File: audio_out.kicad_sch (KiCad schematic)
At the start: 34 parts, among them SW2 Gain0, SW3 Gain1, U3 AP7333-33SR, U4 PCM5102A, U5 PAM8908JER

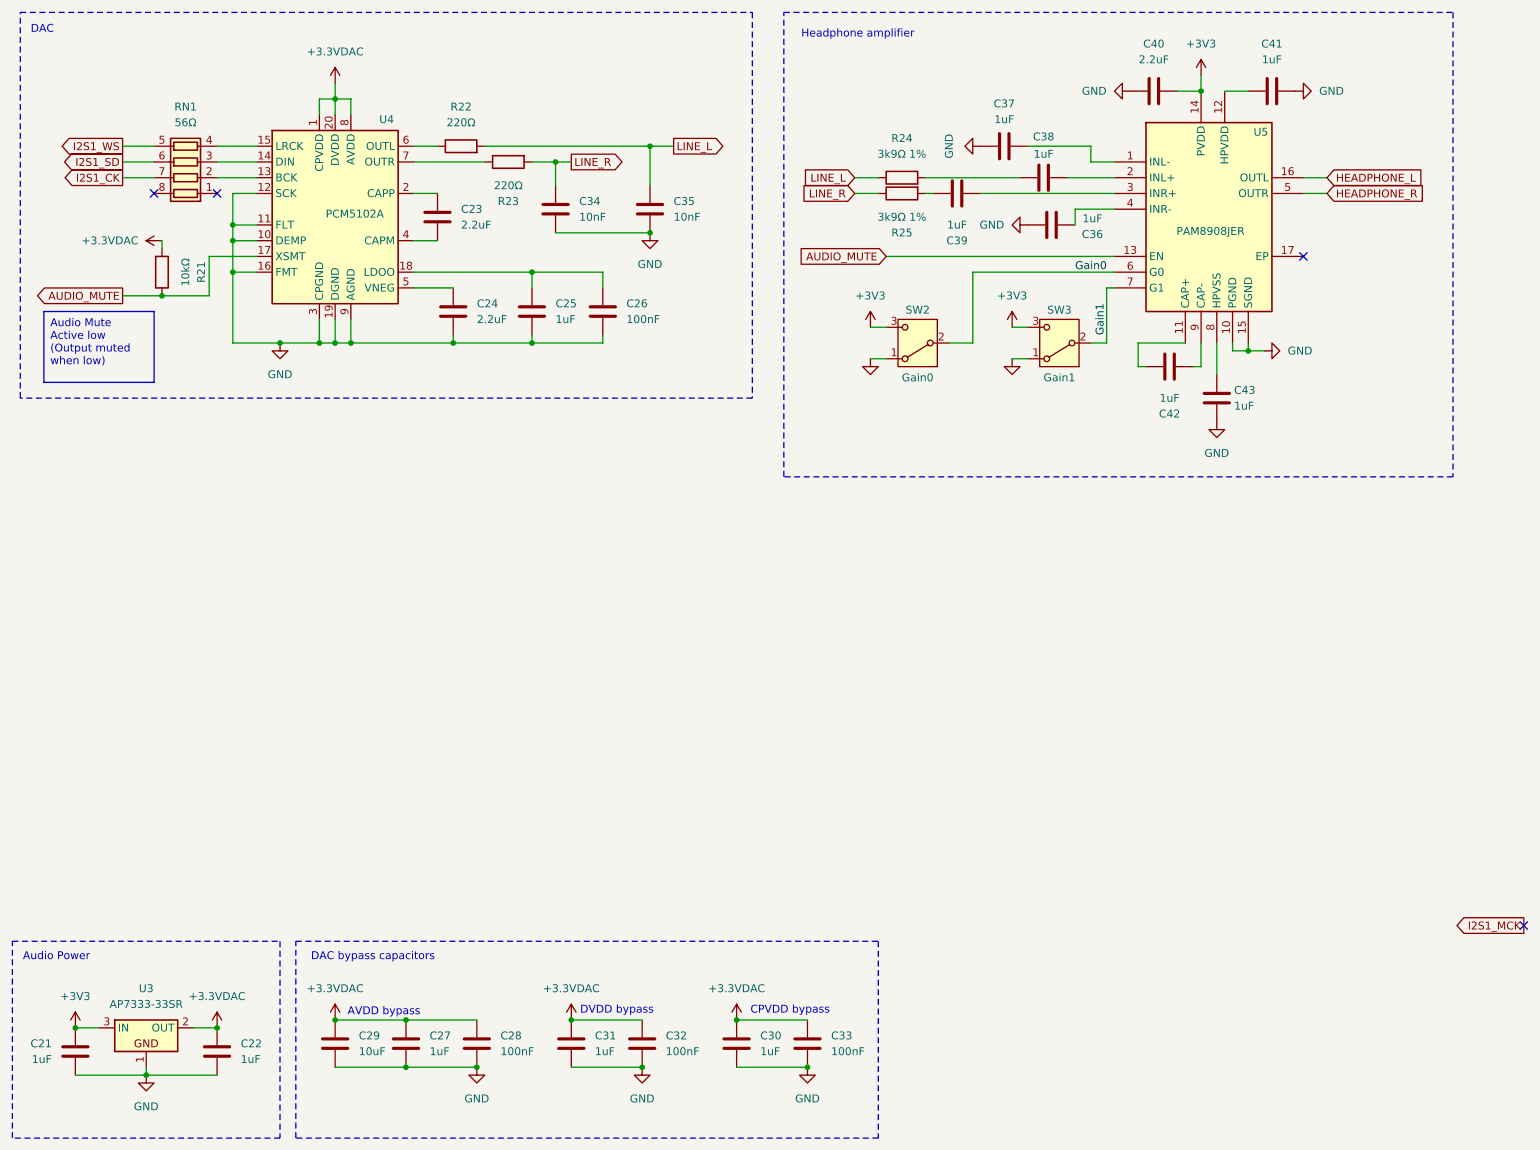
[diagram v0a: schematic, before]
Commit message: Updated schematic with parts found in JLCPCB parts database. Updated footprints, 3d models for those items. All schematic symbols now have LCSC part numbers, footprints and 3D models. No PCB layout has been done.
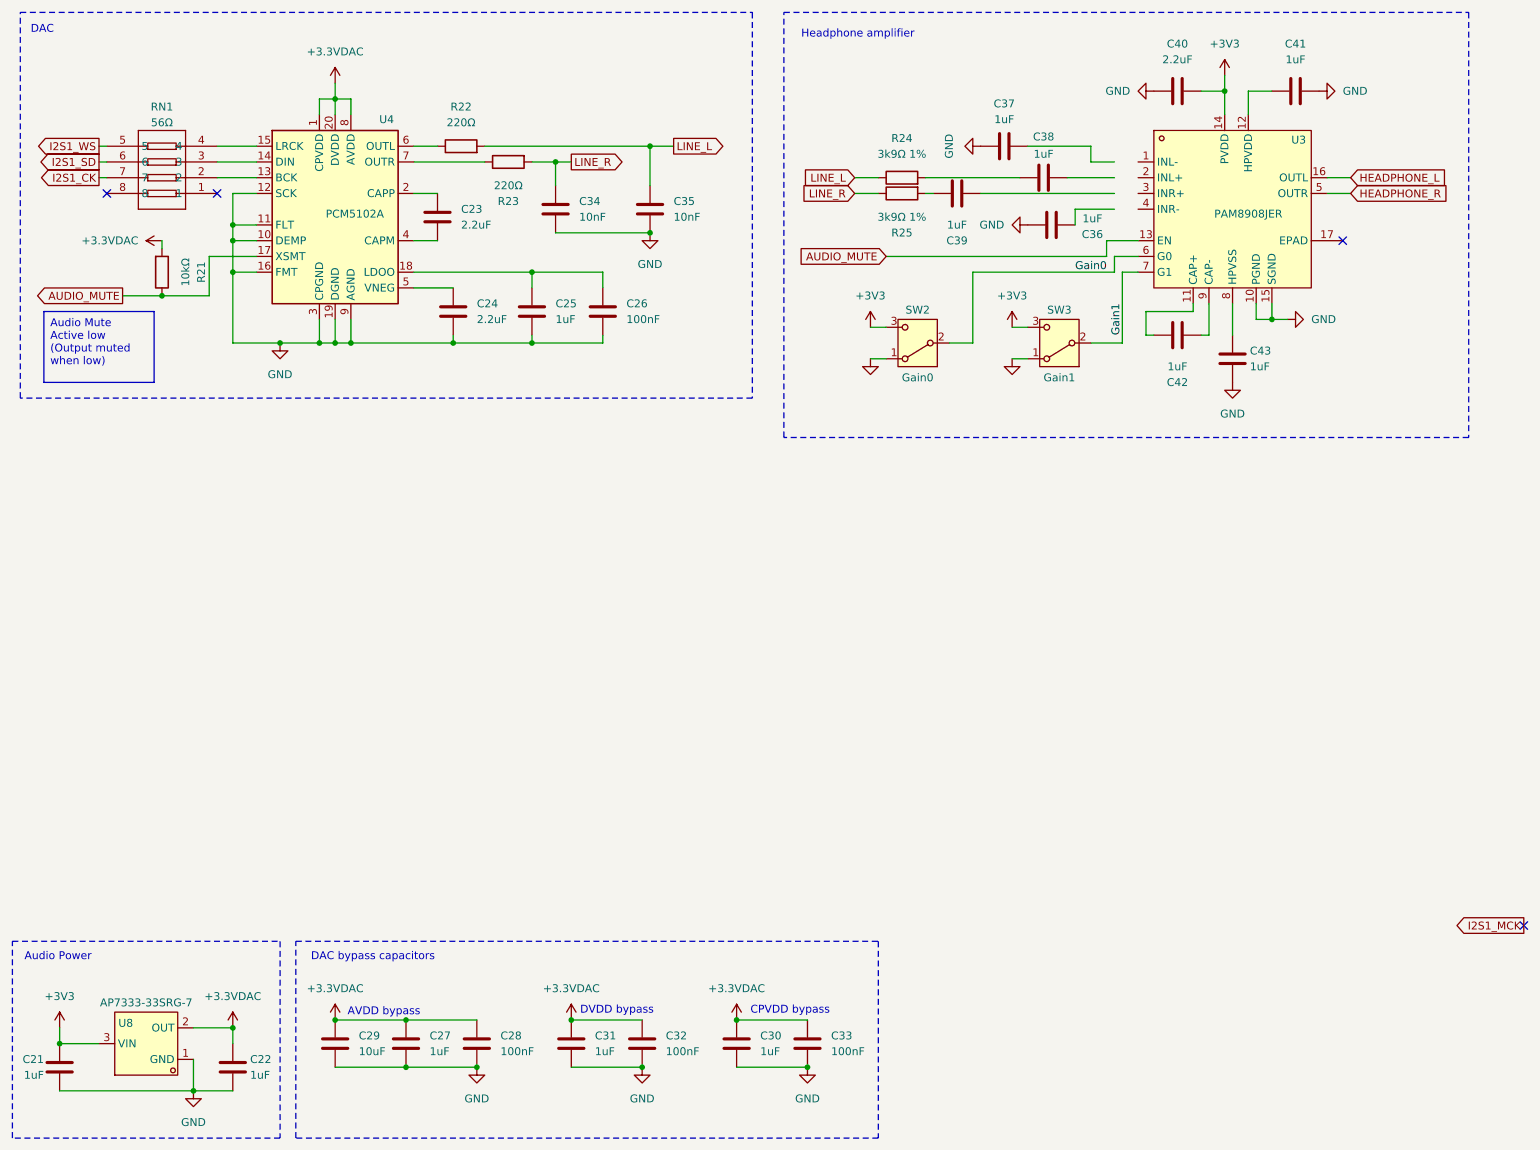
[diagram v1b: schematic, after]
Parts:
- removed RN1: 56Ω, PCM_Resistor_SMD_AKL:R_Array_Convex_4x0603, symbol PCM_Resistor_AKL:R_4x0603_Convex
- removed U3: AP7333-33SR, PCM_Package_TO_SOT_SMD_AKL:SOT-23, symbol PCM_Voltage_Regulator_AKL:AP7333-33SR
- removed U5: PAM8908JER, QFN50P300X300X65-17N, symbol PAM8908JER:PAM8908JER
- added RN1: 56Ω, easyeda2kicad:RES-ARRAY-SMD_0603-8P-L3.2-W1.6-BL, symbol easyeda2kicad:4D03WGJ0560T5E
- added U3: PAM8908JER, easyeda2kicad:QFN-16_L3.0-W3.0-P0.50-BL-EP1.7, symbol easyeda2kicad:PAM8908JER
- added U8: AP7333-33SRG-7, easyeda2kicad:SOT-23-3_L2.9-W1.3-P1.90-LS2.4-BR, symbol easyeda2kicad:AP7333-33SRG-7
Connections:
- net +3.3VDAC: now also U8.2 (OUT)
- net +3V3: now also U3.14 (PVDD), U8.3 (VIN)
- net AUDIO_MUTE: now also U3.13 (EN)
- net GND: now also U3.10 (PGND), U3.15 (SGND), U8.1 (GND)
- net Gain0: now also U3.6 (G0)
- net Gain1: now also U3.7 (G1)
- net HEADPHONE_L: now also U3.16 (OUTL)
- net HEADPHONE_R: now also U3.5 (OUTR)
- net I2S1_CK: now also RN1.7
- net I2S1_SD: now also RN1.6
- net I2S1_WS: now also RN1.5
- net at U4.13 (BCK): now also RN1.2
- net at U4.14 (DIN): now also RN1.3
- net at U4.15 (LRCK): now also RN1.4
- net at C42.2: now also U3.11 (CAP+)
- net at C41.1: now also U3.12 (HPVDD)
- net at C43.1: now also U3.8 (HPVSS)
- net at C42.1: now also U3.9 (CAP-)
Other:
- moved on the sheet: C21, C22, C40, C41, C42, C43

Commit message: Group PCB components together more. Replace 2x2x4 by 1x2x8 connector.
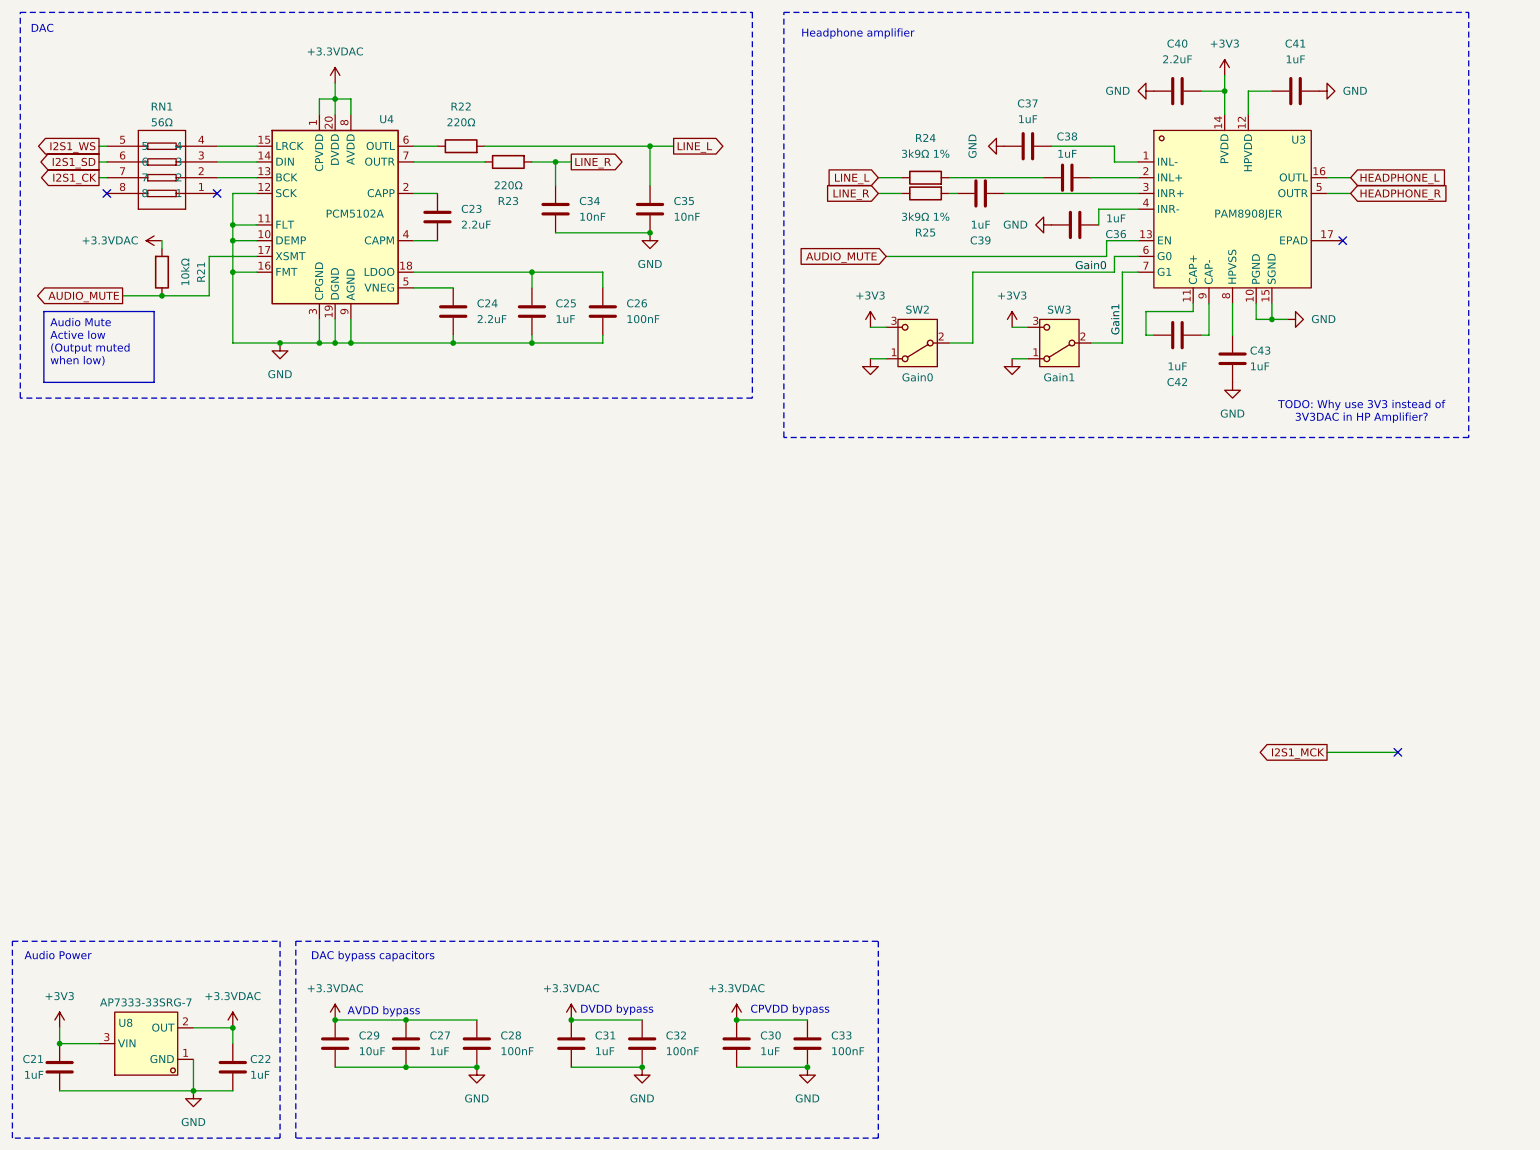
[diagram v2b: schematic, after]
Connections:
- net at C39.2: now also U3.3 (INR+)
- net at C37.2: now also U3.1 (INL-)
- net at C36.2: now also U3.4 (INR-)
- net at C38.2: now also U3.2 (INL+)
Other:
- note added: "TODO: Why use 3V3 instead of 3V3DAC in HP Amplifier?"
- moved on the sheet: C36, C37, C38, C39, R24, R25

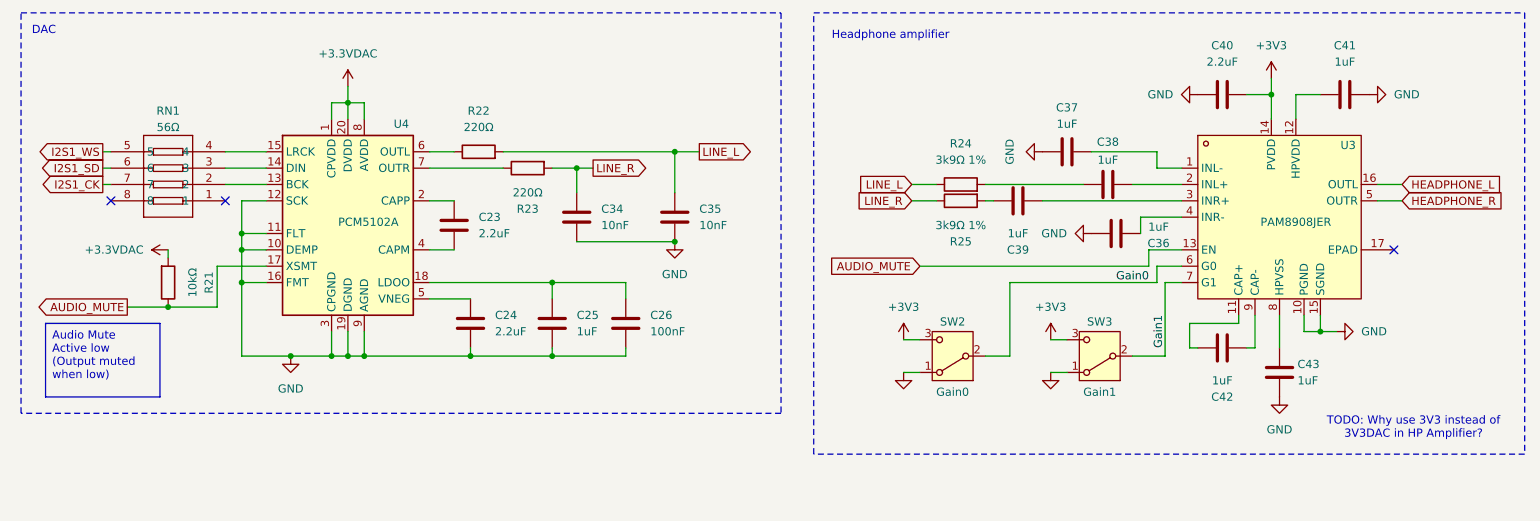
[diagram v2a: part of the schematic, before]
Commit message: Ready to start routing the PCB I think
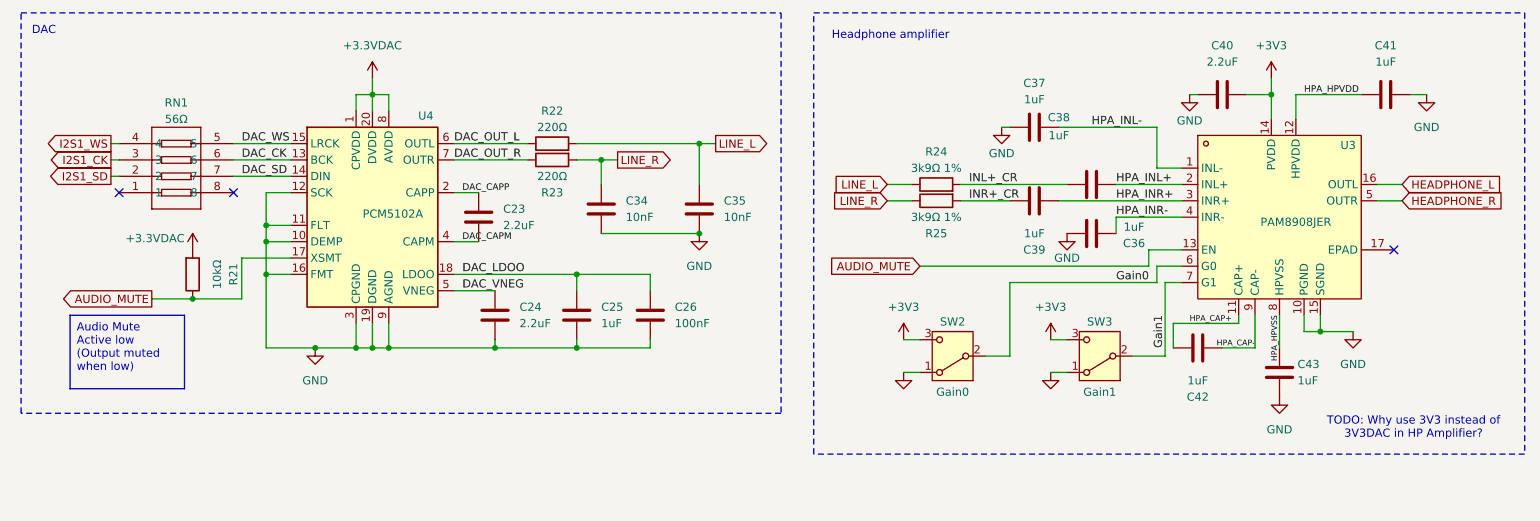
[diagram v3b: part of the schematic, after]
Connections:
- net I2S1_CK: now also RN1.3; no longer RN1.7
- net I2S1_SD: now also RN1.2; no longer RN1.6
- net I2S1_WS: now also RN1.4; no longer RN1.5
- net INR+_CR: now reaches C39.1, R25.2
- net INL+_CR: now reaches C38.1, R24.2
- net HPA_INR+: now reaches C39.2, U3.3 (INR+)
- net DAC_CK: now reaches U4.13 (BCK)
- net DAC_CK: now also RN1.6; no longer RN1.2
- net DAC_SD: now reaches U4.14 (DIN)
- net DAC_SD: now also RN1.7; no longer RN1.3
- net DAC_WS: now reaches U4.15 (LRCK)
- net DAC_WS: now also RN1.5; no longer RN1.4
- net DAC_LDOO: now reaches C25.1, C26.1, U4.18 (LDOO)
- net DAC_CAPP: now reaches C23.1, U4.2 (CAPP)
- net DAC_CAPM: now reaches C23.2, U4.4 (CAPM)
- net DAC_VNEG: now reaches C24.1, U4.5 (VNEG)
- net DAC_OUT_L: now reaches R22.1, U4.6 (OUTL)
- net DAC_OUT_R: now reaches R23.1, U4.7 (OUTR)
- net HPA_INL-: now reaches C37.2, U3.1 (INL-)
- net HPA_HPVSS: now reaches C43.1, U3.8 (HPVSS)
- net HPA_INR-: now reaches C36.2, U3.4 (INR-)
- net HPA_CAP-: now reaches C42.1, U3.9 (CAP-)
- net HPA_CAP+: now reaches C42.2, U3.11 (CAP+)
- net HPA_INL+: now reaches C38.2, U3.2 (INL+)
- net HPA_HPVDD: now reaches C41.1, U3.12 (HPVDD)
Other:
- moved on the sheet: C23, C24, C25, C26, C34, C35, C36, C37, C38, C39, C41, C42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

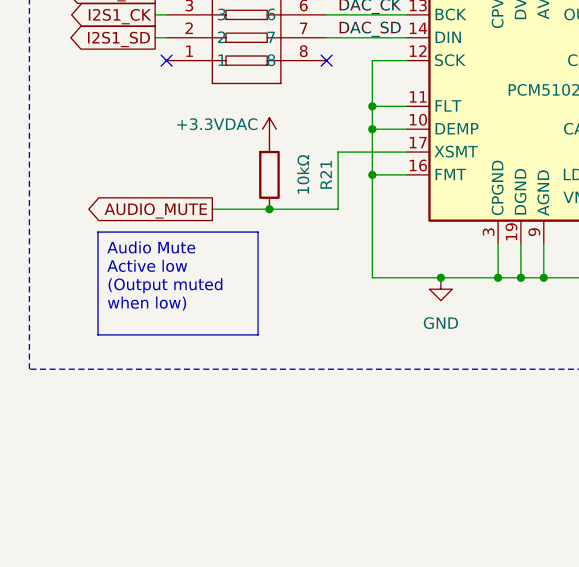
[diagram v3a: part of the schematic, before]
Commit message: Connected the two crystals
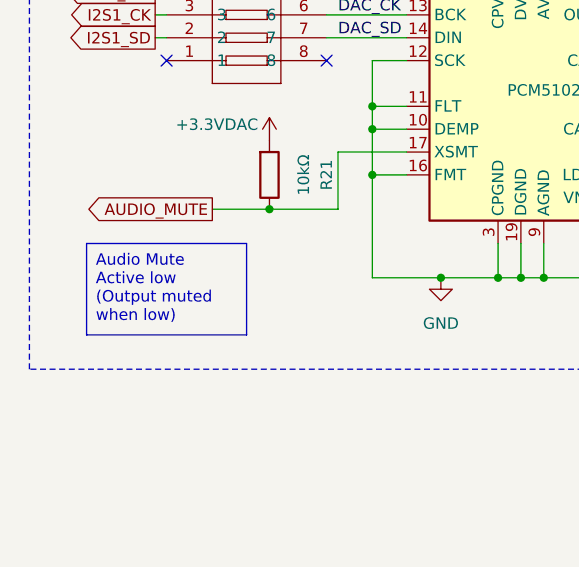
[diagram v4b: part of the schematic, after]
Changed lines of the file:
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@@
 	(text_box "Audio Mute\nActive low\n(Output muted \nwhen low)"
 		(exclude_from_sim no)
-		(at 25.4 64.77 0)
-		(size 17.78 11.43)
+		(at 24.13 66.04 0)
+		(size 17.78 10.16)
 		(stroke
 			(width 0)
